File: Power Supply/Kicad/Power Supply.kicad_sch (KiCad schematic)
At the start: 28 parts, among them J1 Conn_02x05_Counter_Clockwise, J2 PJ-082BH, U1 LM62440-Q1

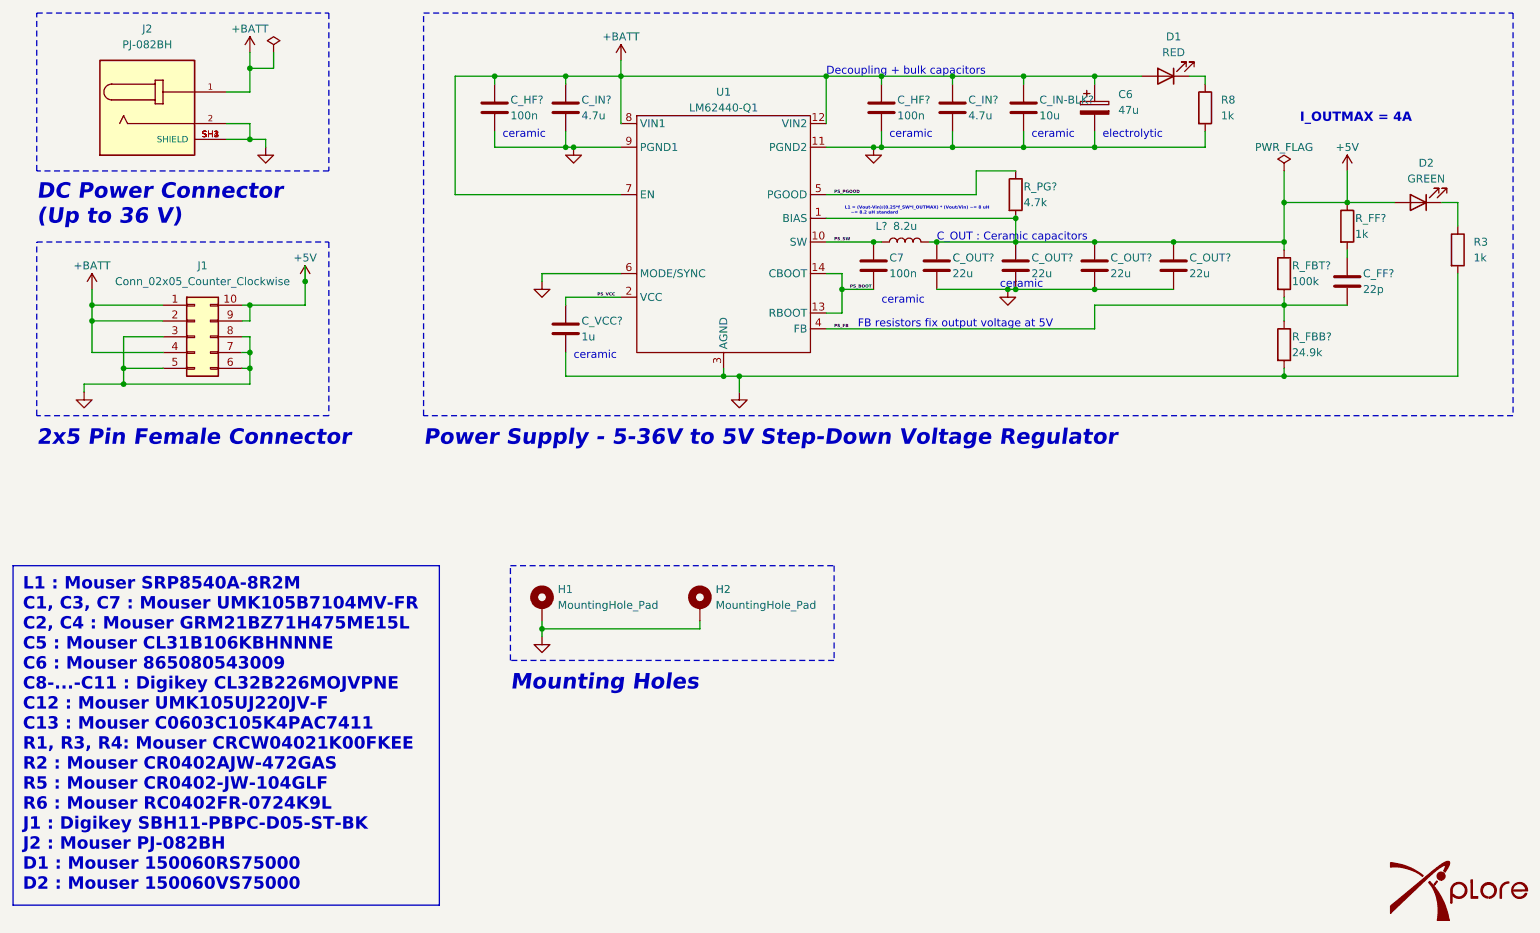
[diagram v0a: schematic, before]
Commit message: added encoders, slightly adjusted copper tracks
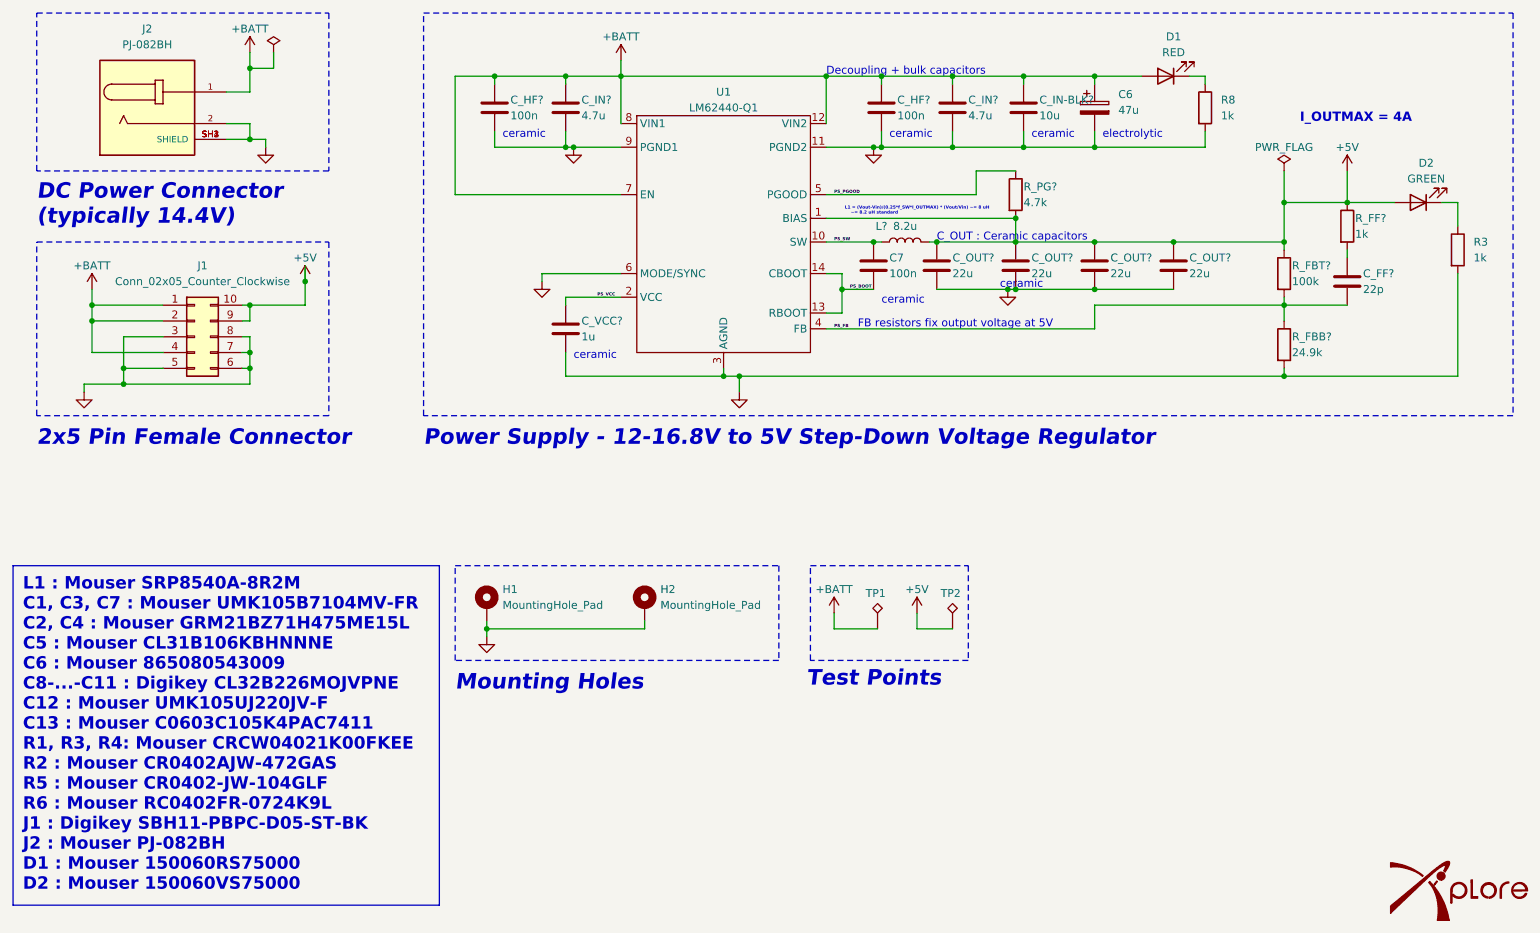
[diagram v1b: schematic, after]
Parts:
- added TP1, TP2: TestPoint_Alt, TestPoint:TestPoint_Pad_2.0x2.0mm, symbol Connector:TestPoint_Alt
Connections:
- net +5V: now also TP2.1
- net +BATT: now also TP1.1
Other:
- note added: "DC Power Connector (typically 14.4V)"
- note added: "Power Supply - 12-16.8V to 5V Step-Down Voltage Regulator"
- note added: "Test Points"
- note removed: "DC Power Connector (Up to 36 V)"
- note removed: "Power Supply - 5-36V to 5V Step-Down Voltage Regulator"
- moved on the sheet: H1, H2
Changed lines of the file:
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@@
   (junction (at 45.72 90.17) (diameter 0) (color 0 0 0 0)
   )
-  (junction (at 113.03 132.08) (diameter 0) (color 0 0 0 0)
+  (junction (at 104.14 132.08) (diameter 0) (color 0 0 0 0)
   )
   (junction (at 201.93 69.85) (diameter 0) (color 0 0 0 0)
@@
     (stroke (width 0) (type default))
   )
-  (wire (pts (xy 113.03 132.08) (xy 138.43 132.08))
+  (wire (pts (xy 104.14 132.08) (xy 129.54 132.08))
     (stroke (width 0) (type default))
   )
@@
     (stroke (width 0) (type default))
   )
-  (wire (pts (xy 113.03 132.08) (xy 113.03 133.35))
+  (wire (pts (xy 104.14 132.08) (xy 104.14 133.35))
     (stroke (width 0) (type default))
   )
@@
     (stroke (width 0) (type default))
   )
-  (wire (pts (xy 113.03 130.81) (xy 113.03 132.08))
+  (wire (pts (xy 104.14 130.81) (xy 104.14 132.08))
     (stroke (width 0) (type default))
   )
@@
     (stroke (width 0) (type default))
   )
+  (wire (pts (xy 160.02 132.08) (xy 167.005 132.08))
+    (stroke (width 0) (type default))
+  )
   (wire (pts (xy 187.96 77.47) (xy 189.23 77.47))
     (stroke (width 0) (type default))
@@
     (stroke (width 0) (type default))
   )
+  (wire (pts (xy 160.02 129.54) (xy 160.02 132.08))
+    (stroke (width 0) (type default))
+  )
   (wire (pts (xy 66.04 45.72) (xy 62.23 45.72))
     (stroke (width 0) (type default))
@@
     (stroke (width 0) (type default))
   )
+  (wire (pts (xy 173.355 132.08) (xy 179.07 132.08))
+    (stroke (width 0) (type default))
+  )
   (wire (pts (xy 116.84 78.74) (xy 116.84 80.01))
     (stroke (width 0) (type default))
@@
     (stroke (width 0) (type default))
   )
-  (wire (pts (xy 138.43 130.81) (xy 138.43 132.08))
+  (wire (pts (xy 129.54 130.81) (xy 129.54 132.08))
     (stroke (width 0) (type default))
   )
@@
     (stroke (width 0) (type default))
   )
+  (wire (pts (xy 173.355 129.54) (xy 173.355 132.08))
+    (stroke (width 0) (type default))
+  )
   (wire (pts (xy 176.53 77.47) (xy 187.96 77.47))
     (stroke (width 0) (type default))
@@
     (stroke (width 0) (type default))
   )
-  (rectangle (start 107.95 121.92) (end 160.02 137.16)
+  (rectangle (start 99.06 121.92) (end 151.13 137.16)
     (stroke (width 0.2) (type dash))
     (fill (type none))
@@
     (fill (type none))
   )
+  (rectangle (start 156.21 121.92) (end 181.61 137.16)
+    (stroke (width 0.2) (type dash))
+    (fill (type none))
+  )
   (rectangle (start 31.75 69.85) (end 78.74 97.79)
     (stroke (width 0.2) (type dash))
@@
     (effects (font (size 1.27 1.27)) (justify left bottom))
   )
-  (text "DC Power Connector \n(Up to 36 V)" (at 31.75 67.31 0)
+  (text "DC Power Connector \n(typically 14.4V)" (at 31.75 67.31 0)
     (effects (font (size 2.5 2.5) (thickness 0.5) bold italic (color 0 0 0 1)) (justify left bottom))
   )
@@
     (effects (font (size 1.27 1.27)) (justify left bottom))
   )
-  (text "Power Supply - 5-36V to 5V Step-Down Voltage Regulator "
+  (text "Power Supply - 12-16.8V to 5V Step-Down Voltage Regulator"
     (at 93.98 102.87 0)
     (effects (font (size 2.5 2.5) (thickness 0.5) bold italic (color 0 0 0 1)) (justify left bottom))
   )
+  (text "Test Points" (at 155.575 141.605 0)
+    (effects (font (size 2.5 2.5) (thickness 0.5) bold italic (color 0 0 0 1)) (justify left bottom))
+  )
   (text "ceramic" (at 186.69 77.47 0)
     (effects (font (size 1.27 1.27)) (justify left bottom))
@@
     (effects (font (size 1.27 1.27)) (justify left bottom))
   )
-  (text "Mounting Holes" (at 107.95 142.24 0)
+  (text "Mounting Holes" (at 99.06 142.24 0)
     (effects (font (size 2.5 2.5) (thickness 0.5) bold italic (color 0 0 0 1)) (justify left bottom))
   )
@@
     )
   )
-  (symbol (lib_id "power:GND") (at 113.03 133.35 0) (unit 1)
+  (symbol (lib_id "Connector:TestPoint_Alt") (at 179.07 132.08 0) (unit 1)
+    (in_bom yes) (on_board yes) (dnp no)
+    (property "Reference" "TP2" (at 177.165 126.365 0)
+      (effects (font (size 1.27 1.27)) (justify left))
+    )
+    (property "Value" "TestPoint_Alt" (at 180.975 130.048 0)
+      (effects (font (size 1.27 1.27)) (justify left) hide)
+    )
+    (property "Footprint" "TestPoint:TestPoint_Pad_2.0x2.0mm" (at 184.15 132.08 0)
+      (effects (font (size 1.27 1.27)) hide)
+    )
+    (property "Datasheet" "~" (at 184.15 132.08 0)
+      (effects (font (size 1.27 1.27)) hide)
+    )
+    (pin "1")
+    (instances
+      (project "Power Supply"
+        (path "/c3cddd23-9147-41f9-a63c-fa9cc2f58832"
+          (reference "TP2") (unit 1)
+        )
+      )
+    )
+  )
+  (symbol (lib_id "power:GND") (at 104.14 133.35 0) (unit 1)
     (in_bom yes) (on_board yes) (dnp no) (fields_autoplaced)
-    (property "Reference" "#PWR08" (at 113.03 139.7 0)
+    (property "Reference" "#PWR08" (at 104.14 139.7 0)
       (effects (font (size 1.27 1.27)) hide)
     )
-    (property "Value" "GND" (at 113.03 138.43 0)
+    (property "Value" "GND" (at 104.14 138.43 0)
       (effects (font (size 1.27 1.27)) hide)
     )
-    (property "Footprint" "" (at 113.03 133.35 0)
+    (property "Footprint" "" (at 104.14 133.35 0)
       (effects (font (size 1.27 1.27)) hide)
     )
-    (property "Datasheet" "" (at 113.03 133.35 0)
+    (property "Datasheet" "" (at 104.14 133.35 0)
       (effects (font (size 1.27 1.27)) hide)
     )
@@
     )
   )
+  (symbol (lib_id "power:+BATT") (at 160.02 129.54 0) (unit 1)
+    (in_bom yes) (on_board yes) (dnp no)
+    (property "Reference" "#PWR015" (at 160.02 133.35 0)
+      (effects (font (size 1.27 1.27)) hide)
+    )
+    (property "Value" "+BATT" (at 160.02 125.73 0)
+      (effects (font (size 1.27 1.27)))
+    )
+    (property "Footprint" "" (at 160.02 129.54 0)
+      (effects (font (size 1.27 1.27)) hide)
+    )
+    (property "Datasheet" "" (at 160.02 129.54 0)
+      (effects (font (size 1.27 1.27)) hide)
+    )
+    (pin "1")
+    (instances
+      (project "Power Supply"
+        (path "/c3cddd23-9147-41f9-a63c-fa9cc2f58832"
+          (reference "#PWR015") (unit 1)
+        )
+      )
+    )
+  )
   (symbol (lib_id "Device:C") (at 201.93 73.66 0) (unit 1)
     (in_bom yes) (on_board yes) (dnp no)
@@
     )
   )
-  (symbol (lib_id "Mechanical:MountingHole_Pad") (at 113.03 128.27 0) (unit 1)
+  (symbol (lib_id "Mechanical:MountingHole_Pad") (at 104.14 128.27 0) (unit 1)
     (in_bom yes) (on_board yes) (dnp no) (fields_autoplaced)
-    (property "Reference" "H1" (at 115.57 125.73 0)
+    (property "Reference" "H1" (at 106.68 125.73 0)
       (effects (font (size 1.27 1.27)) (justify left))
     )
-    (property "Value" "MountingHole_Pad" (at 115.57 128.27 0)
+    (property "Value" "MountingHole_Pad" (at 106.68 128.27 0)
       (effects (font (size 1.27 1.27)) (justify left))
     )
-    (property "Footprint" "MountingHole:MountingHole_2.2mm_M2_ISO7380_Pad" (at 113.03 128.27 0)
+    (property "Footprint" "MountingHole:MountingHole_2.2mm_M2_ISO7380_Pad" (at 104.14 128.27 0)
       (effects (font (size 1.27 1.27)) hide)
     )
-    (property "Datasheet" "~" (at 113.03 128.27 0)
+    (property "Datasheet" "~" (at 104.14 128.27 0)
       (effects (font (size 1.27 1.27)) hide)
     )
@@
     )
   )
-  (symbol (lib_id "Mechanical:MountingHole_Pad") (at 138.43 128.27 0) (unit 1)
+  (symbol (lib_id "Connector:TestPoint_Alt") (at 167.005 132.08 0) (unit 1)
+    (in_bom yes) (on_board yes) (dnp no)
+    (property "Reference" "TP1" (at 165.1 126.365 0)
+      (effects (font (size 1.27 1.27)) (justify left))
+    )
+    (property "Value" "TestPoint_Alt" (at 168.91 130.048 0)
+      (effects (font (size 1.27 1.27)) (justify left) hide)
+    )
+    (property "Footprint" "TestPoint:TestPoint_Pad_2.0x2.0mm" (at 172.085 132.08 0)
+      (effects (font (size 1.27 1.27)) hide)
+    )
+    (property "Datasheet" "~" (at 172.085 132.08 0)
+      (effects (font (size 1.27 1.27)) hide)
+    )
+    (pin "1")
+    (instances
+      (project "Power Supply"
+        (path "/c3cddd23-9147-41f9-a63c-fa9cc2f58832"
+          (reference "TP1") (unit 1)
+        )
+      )
+    )
+  )
+  (symbol (lib_id "Mechanical:MountingHole_Pad") (at 129.54 128.27 0) (unit 1)
     (in_bom yes) (on_board yes) (dnp no) (fields_autoplaced)
-    (property "Reference" "H2" (at 140.97 125.73 0)
+    (property "Reference" "H2" (at 132.08 125.73 0)
       (effects (font (size 1.27 1.27)) (justify left))
     )
-    (property "Value" "MountingHole_Pad" (at 140.97 128.27 0)
+    (property "Value" "MountingHole_Pad" (at 132.08 128.27 0)
       (effects (font (size 1.27 1.27)) (justify left))
     )
-    (property "Footprint" "MountingHole:MountingHole_2.2mm_M2_ISO7380_Pad" (at 138.43 128.27 0)
+    (property "Footprint" "MountingHole:MountingHole_2.2mm_M2_ISO7380_Pad" (at 129.54 128.27 0)
       (effects (font (size 1.27 1.27)) hide)
     )
-    (property "Datasheet" "~" (at 138.43 128.27 0)
+    (property "Datasheet" "~" (at 129.54 128.27 0)
       (effects (font (size 1.27 1.27)) hide)
     )
@@
         )
       )
+    )
+  )
+  (symbol (lib_id "power:+5V") (at 173.355 129.54 0) (unit 1)
+    (in_bom yes) (on_board yes) (dnp no)
+    (property "Reference" "#PWR05" (at 173.355 133.35 0)
+      (effects (font (size 1.27 1.27)) hide)
+    )
+    (property "Value" "+5V" (at 173.355 125.73 0)
+      (effects (font (size 1.27 1.27)))
+    )
+    (property "Footprint" "" (at 173.355 129.54 0)
+      (effects (font (size 1.27 1.27)) hide)
+    )
+    (property "Datasheet" "" (at 173.355 129.54 0)
+      (effects (font (size 1.27 1.27)) hide)
+    )
+    (pin "1")
+    (instances
+      (project "RoverPCB"
+        (path "/052e469e-2ccb-400e-bf36-44a19a932360/d5d68e58-4b58-44b0-923a-bd07b7aae5f3"
+          (reference "#PWR05") (unit 1)
+        )
+      )
+      (project "Power Supply"
+        (path "/c3cddd23-9147-41f9-a63c-fa9cc2f58832"
+          (reference "#PWR016") (unit 1)
+        )
+      )
